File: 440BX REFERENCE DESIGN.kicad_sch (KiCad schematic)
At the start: 0 parts

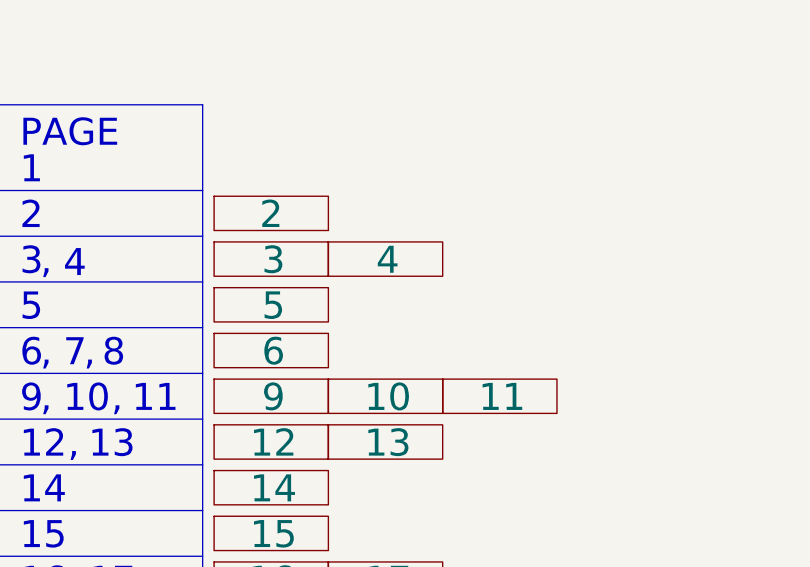
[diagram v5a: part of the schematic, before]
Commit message: page 6,7,8 82443BX chipset, various small fixes
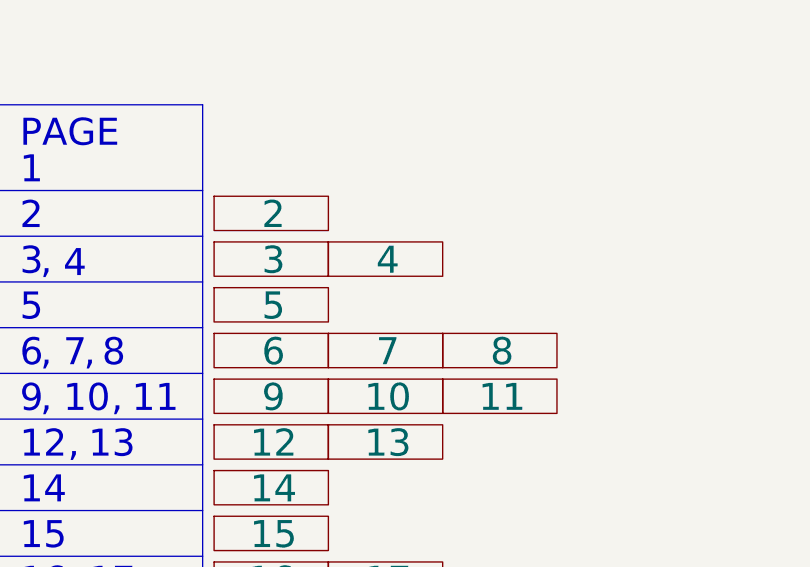
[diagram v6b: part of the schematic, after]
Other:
- sheet 82443BX renamed 82443BX SYSTEM AND DRAM INTERFACES
- added sheet 82443BX MD-HD BUS (82443BX2.kicad_sch)
- added sheet 82443BX PCI AND AGP INTERFACES (82443BX1.kicad_sch)
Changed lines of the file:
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@@
 		)
 		(property "page" "2"
-			(at 142.24 59.182 0)
+			(at 142.494 59.182 0)
 			(effects
 				(font
@@
 			(color 0 0 0 0.0000)
 		)
-		(property "Sheetname" "82443BX"
+		(property "Sheetname" "82443BX SYSTEM AND DRAM INTERFACES"
 			(at 136.144 76.2 0)
 			(effects
@@
 	)
 	(sheet
+		(at 148.59 72.39)
+		(size 12.7 3.81)
+		(exclude_from_sim no)
+		(in_bom yes)
+		(on_board yes)
+		(dnp no)
+		(stroke
+			(width 0.1524)
+			(type solid)
+		)
+		(fill
+			(color 0 0 0 0.0000)
+		)
+		(property "Sheetname" "82443BX PCI AND AGP INTERFACES"
+			(at 148.59 71.6784 0)
+			(effects
+				(font
+					(size 1.27 1.27)
+				)
+				(justify left bottom)
+				(hide yes)
+			)
+		)
+		(property "Sheetfile" "82443BX1.kicad_sch"
+			(at 148.59 76.7846 0)
+			(effects
+				(font
+					(size 1.27 1.27)
+				)
+				(justify left top)
+				(hide yes)
+			)
+		)
+		(property "page" "7"
+			(at 155.194 74.422 0)
+			(effects
+				(font
+					(size 3 3)
+				)
+			)
+		)
+		(instances
+			(project "440BX REFERENCE DESIGN"
+				(path "/373c3af7-3bc7-49b4-93d6-3114ef59c408"
+					(page "7")
+				)
+			)
+		)
+	)
+	(sheet
 		(at 135.89 92.71)
 		(size 12.7 3.81)
@@
 				)
 			)
+		)
+	)
+	(sheet
+		(at 161.29 72.39)
+		(size 12.7 3.81)
+		(exclude_from_sim no)
+		(in_bom yes)
+		(on_board yes)
+		(dnp no)
+		(stroke
+			(width 0.1524)
+			(type solid)
+		)
+		(fill
+			(color 0 0 0 0.0000)
+		)
+		(property "Sheetname" "82443BX MD-HD BUS"
+			(at 161.29 71.6784 0)
+			(effects
+				(font
+					(size 1.27 1.27)
+				)
+				(justify left bottom)
+				(hide yes)
+			)
+		)
+		(property "Sheetfile" "82443BX2.kicad_sch"
+			(at 161.29 76.7846 0)
+			(effects
+				(font
+					(size 1.27 1.27)
+				)
+				(justify left top)
+				(hide yes)
+			)
+		)
+		(property "page" "8"
+			(at 167.894 74.422 0)
+			(effects
+				(font
+					(size 3 3)
+				)
+			)
+		)
+		(instances
+			(project "440BX REFERENCE DESIGN"
+				(path "/373c3af7-3bc7-49b4-93d6-3114ef59c408"
+					(page "8")
+				)
+			)
